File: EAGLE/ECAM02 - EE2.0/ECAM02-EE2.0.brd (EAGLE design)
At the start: 160 x 100 mm, 50 parts, among them J1 MODULAR TOOL, J2 SPI, J3 MOT, J4 FTDI, J5 S4B-PH-SM4, J6 S5B-PH-SM, J7 RINGLIGHT, Q2 16MHz, U1 SP3485, U2 ATMEGA238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

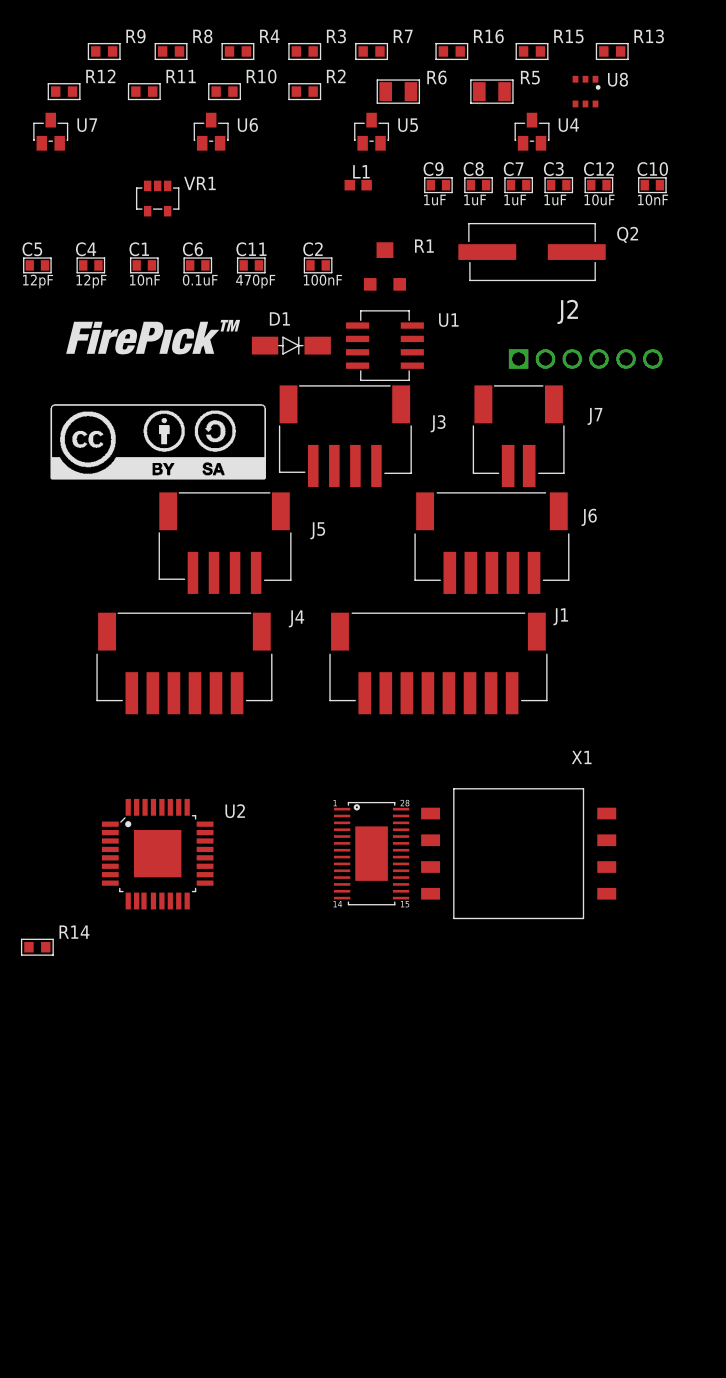
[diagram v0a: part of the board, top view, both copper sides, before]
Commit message: Finalized schematics (minus potential LDO regulator) for all boards. Layout partially done for EFD01
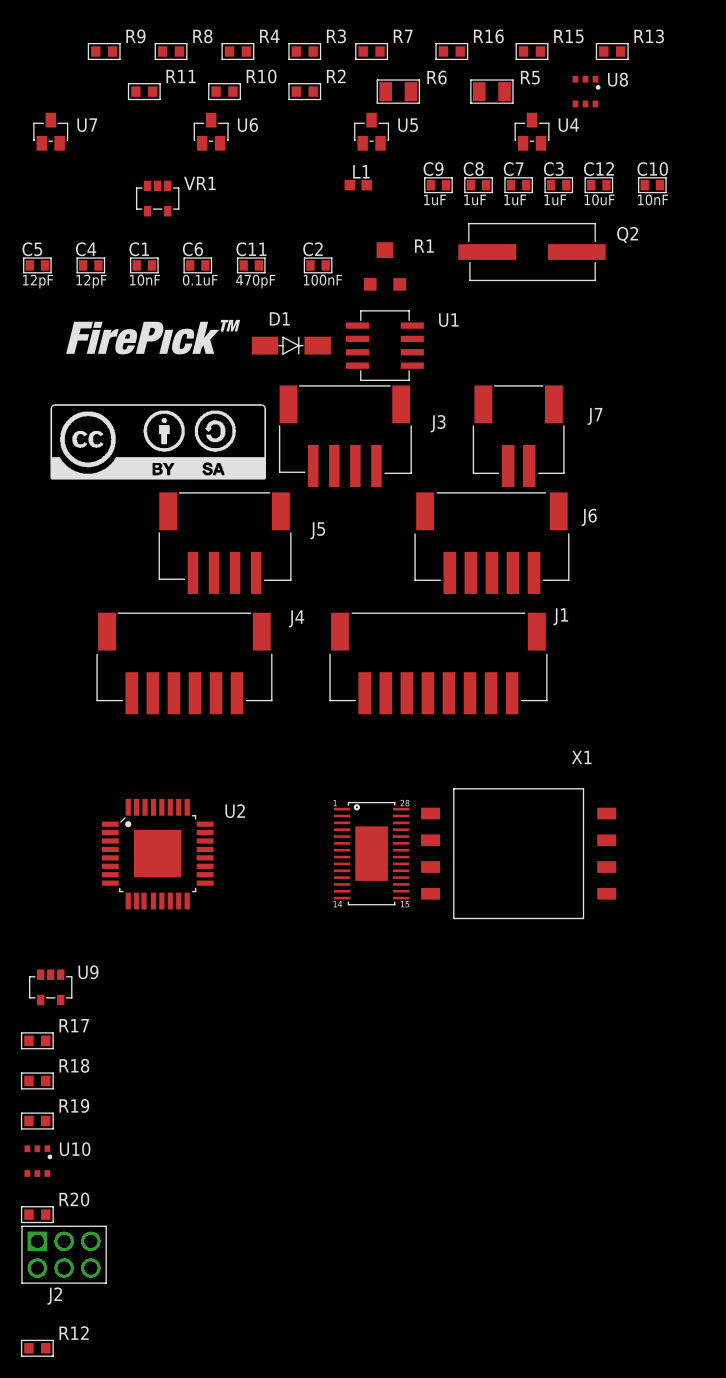
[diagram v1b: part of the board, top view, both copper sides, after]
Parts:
- removed R14: 10K, TinWhiskers:R0603
- added R17: 10R, TinWhiskers:R0603
- added R18, R20: 5K, TinWhiskers:R0603
- added R19: 90K, TinWhiskers:R0603
- added U10: MCP4725, TinWhiskers:SOT-23-6
- added U9: OR(74LVC), TinWhiskers:SOT-23-5
- J2: device TinWhiskers:CON-HDR-6POS-MALE -> TinWhiskers:CON-HDR-2X3P
- moved R12 119.4 mm to (-73.7, -40.6)
- moved J2 98.5 mm to (-71.1, -31.8)
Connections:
- removed net !ENBL: U2.9, U3.21
- removed net FB: J7.2, U8.3
- removed net SS: R14.2, U2.14
- new net !ENBL_AVR: U2.26, U9.2
- new net !ENBL_MOD: J1.2, U9.1
- new net A0: R19.1, U10.6
- new net N$10: R20.2, U10.1
- new net N$3: J7.2, R17.2, R18.2
- new net N$4: R18.1, R19.2, U8.3
- new net SCL: U10.5, U2.28
- new net SDA: U10.4, U2.27
- net !ENABLE: now also U3.21, U9.4; no longer J1.2
- net +3V3: now also U9.5
- net +5V: now also U10.3; no longer R14.1
- net CTRL: now also U2.11
- net DIR: now also U2.25
- net GATE1: now also U2.1; no longer U2.24
- net GATE2: now also U2.9; no longer U2.25
- net GATE3: now also U2.10; no longer U2.26
- net GATE4: now also U2.13; no longer U2.27
- net GND: now also R17.1, R20.1, U10.2, U9.3
- net STEP: now also U2.24; no longer U2.1

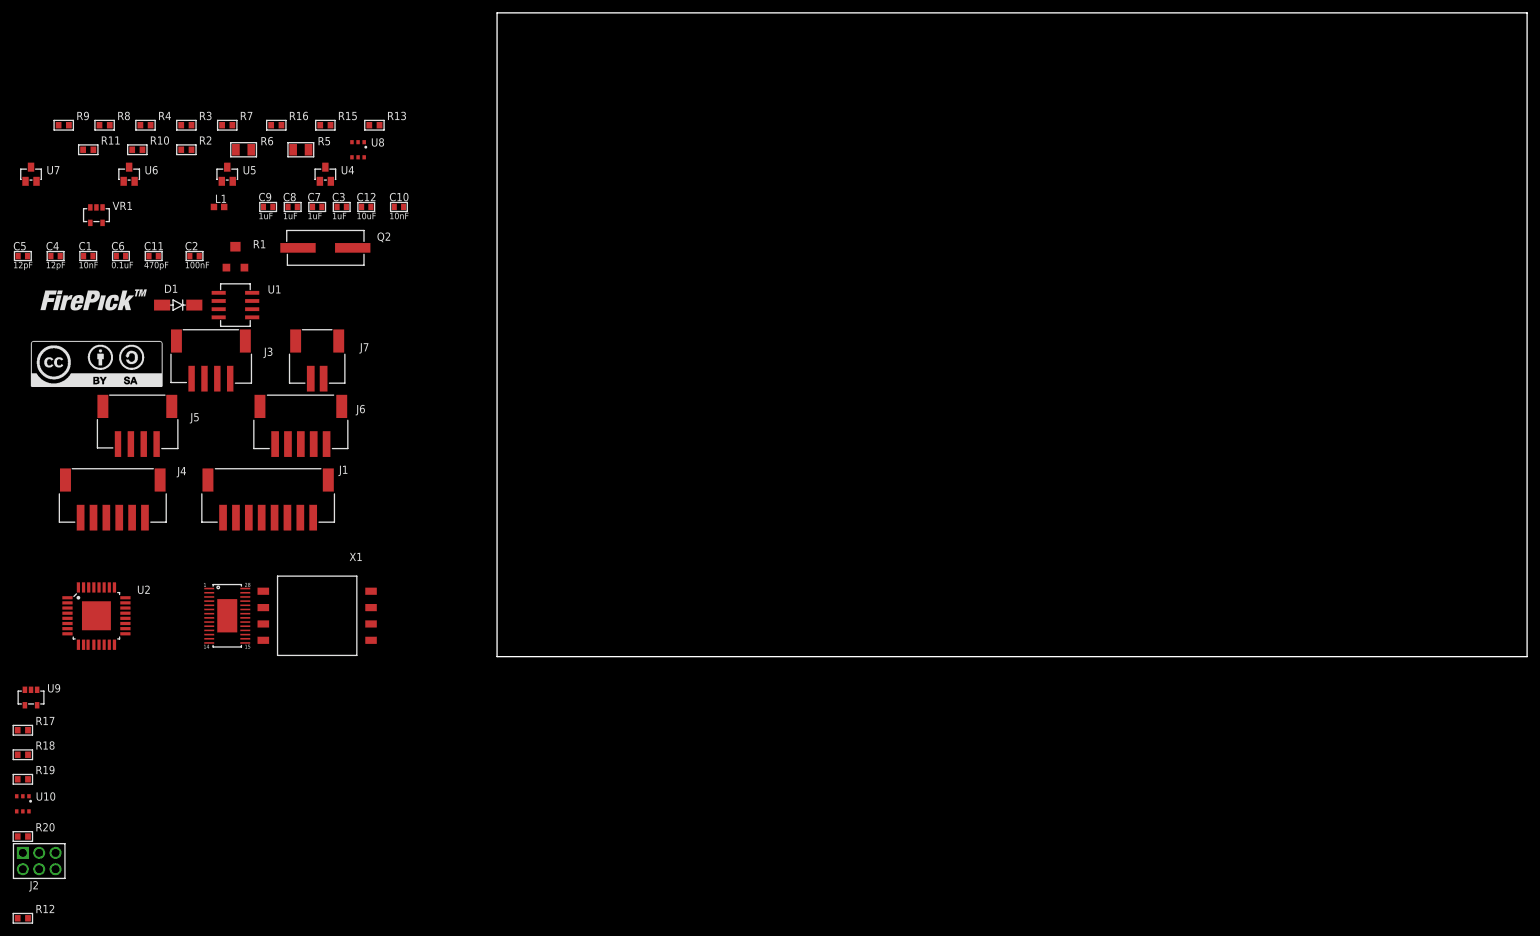
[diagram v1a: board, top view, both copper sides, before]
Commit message: Routed EFD01, ECAM03 boards. Modification needs to be made for hole/keepout in ECAM03. EMC03 X and Y sides routed. Will need to increase some trace widths.
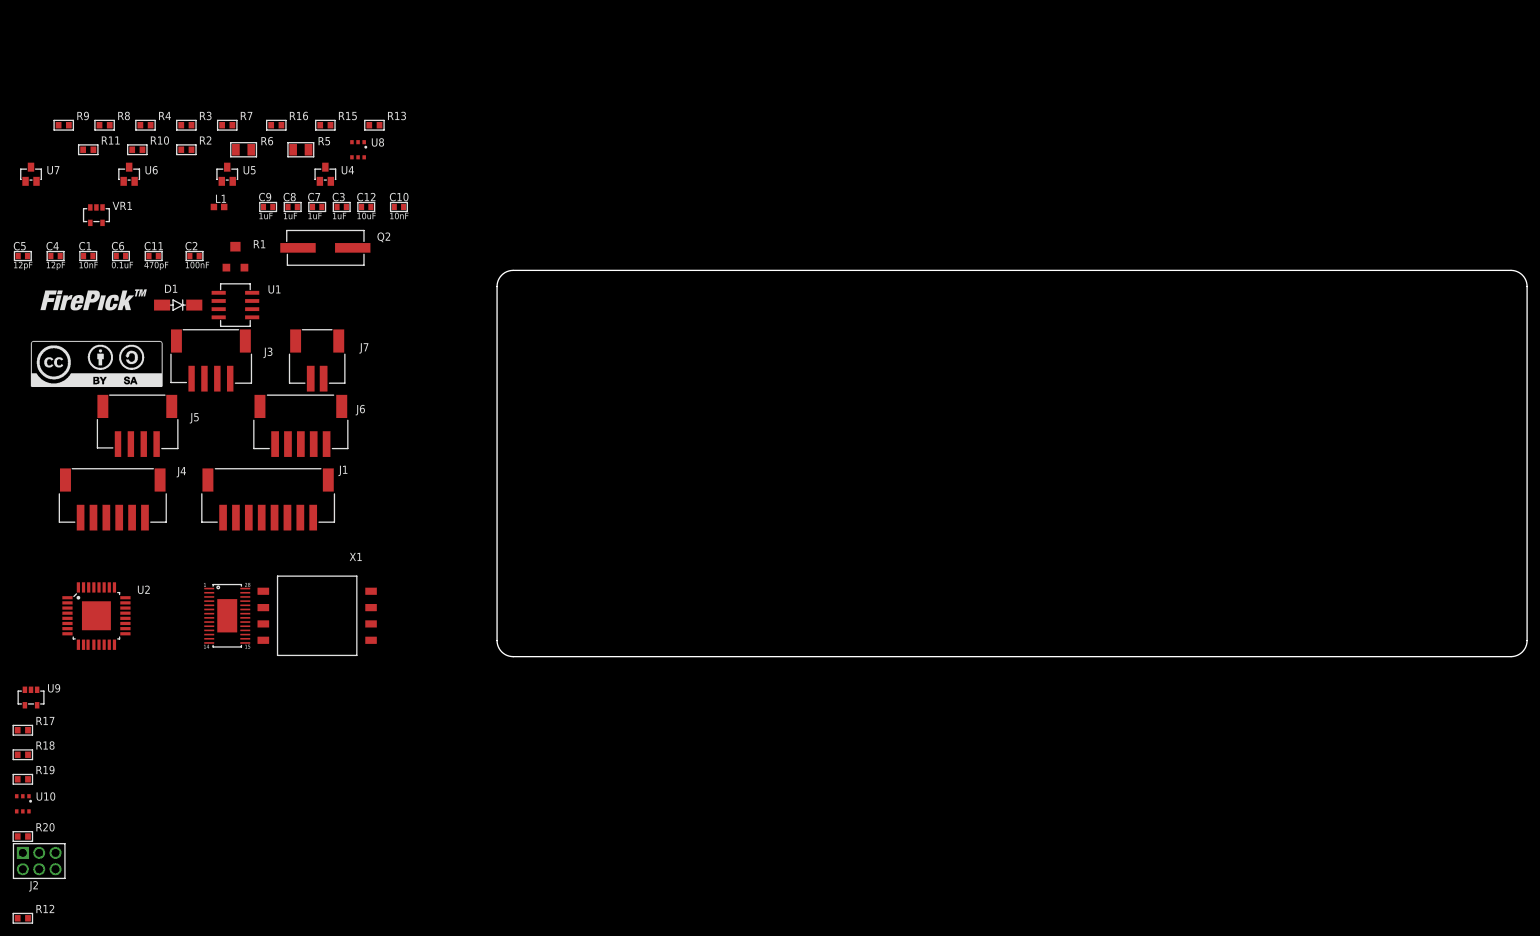
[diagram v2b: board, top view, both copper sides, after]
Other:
- board size 160 x 100 mm -> 160 x 60 mm
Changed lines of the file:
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@@
 <setting verticaltext="up"/>
 </settings>
-<grid distance="0.05" unitdist="inch" unit="inch" style="lines" multiple="1" display="no" altdistance="0.025" altunitdist="inch" altunit="inch"/>
+<grid distance="0.1" unitdist="mm" unit="mm" style="lines" multiple="1" display="no" altdistance="0.025" altunitdist="inch" altunit="mm"/>
 <layers>
 <layer number="1" name="Top" color="4" fill="1" visible="yes" active="yes"/>
@@
 <layer number="43" name="vRestrict" color="2" fill="10" visible="yes" active="yes"/>
 <layer number="44" name="Drills" color="7" fill="1" visible="no" active="yes"/>
-<layer number="45" name="Holes" color="7" fill="1" visible="no" active="yes"/>
+<layer number="45" name="Holes" color="7" fill="1" visible="yes" active="yes"/>
 <layer number="46" name="Milling" color="3" fill="1" visible="no" active="yes"/>
 <layer number="47" name="Measures" color="7" fill="1" visible="no" active="yes"/>
@@
 <board>
 <plain>
-<wire x1="0" y1="0" x2="160" y2="0" width="0" layer="20"/>
-<wire x1="160" y1="0" x2="160" y2="100" width="0" layer="20"/>
-<wire x1="160" y1="100" x2="0" y2="100" width="0" layer="20"/>
-<wire x1="0" y1="100" x2="0" y2="0" width="0" layer="20"/>
+<wire x1="0" y1="57.5" x2="0" y2="2.5" width="0.01" layer="20"/>
+<wire x1="0" y1="2.5" x2="2.5" y2="0" width="0.01" layer="20" curve="90"/>
+<wire x1="2.5" y1="0" x2="157.5" y2="0" width="0.01" layer="20"/>
+<wire x1="157.5" y1="0" x2="160" y2="2.5" width="0.01" layer="20" curve="90"/>
+<wire x1="160" y1="2.5" x2="160" y2="57.5" width="0.01" layer="20"/>
+<wire x1="160" y1="57.5" x2="157.5" y2="60" width="0.01" layer="20" curve="90"/>
+<wire x1="157.5" y1="60" x2="2.5" y2="60" width="0.01" layer="20"/>
+<wire x1="2.5" y1="60" x2="0" y2="57.5" width="0.01" layer="20" curve="90"/>
+<polygon width="0.01" layer="39">
+<vertex x="62.5" y="12.5"/>
+<vertex x="97.5" y="12.5"/>
+<vertex x="97.5" y="47.5"/>
+<vertex x="62.5" y="47.5"/>
+</polygon>
 </plain>
 <attributes>

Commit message: Routed all boards. EFP01 has a serious problem with spacing. Even on minimum allowable there are 300 DRC errors.
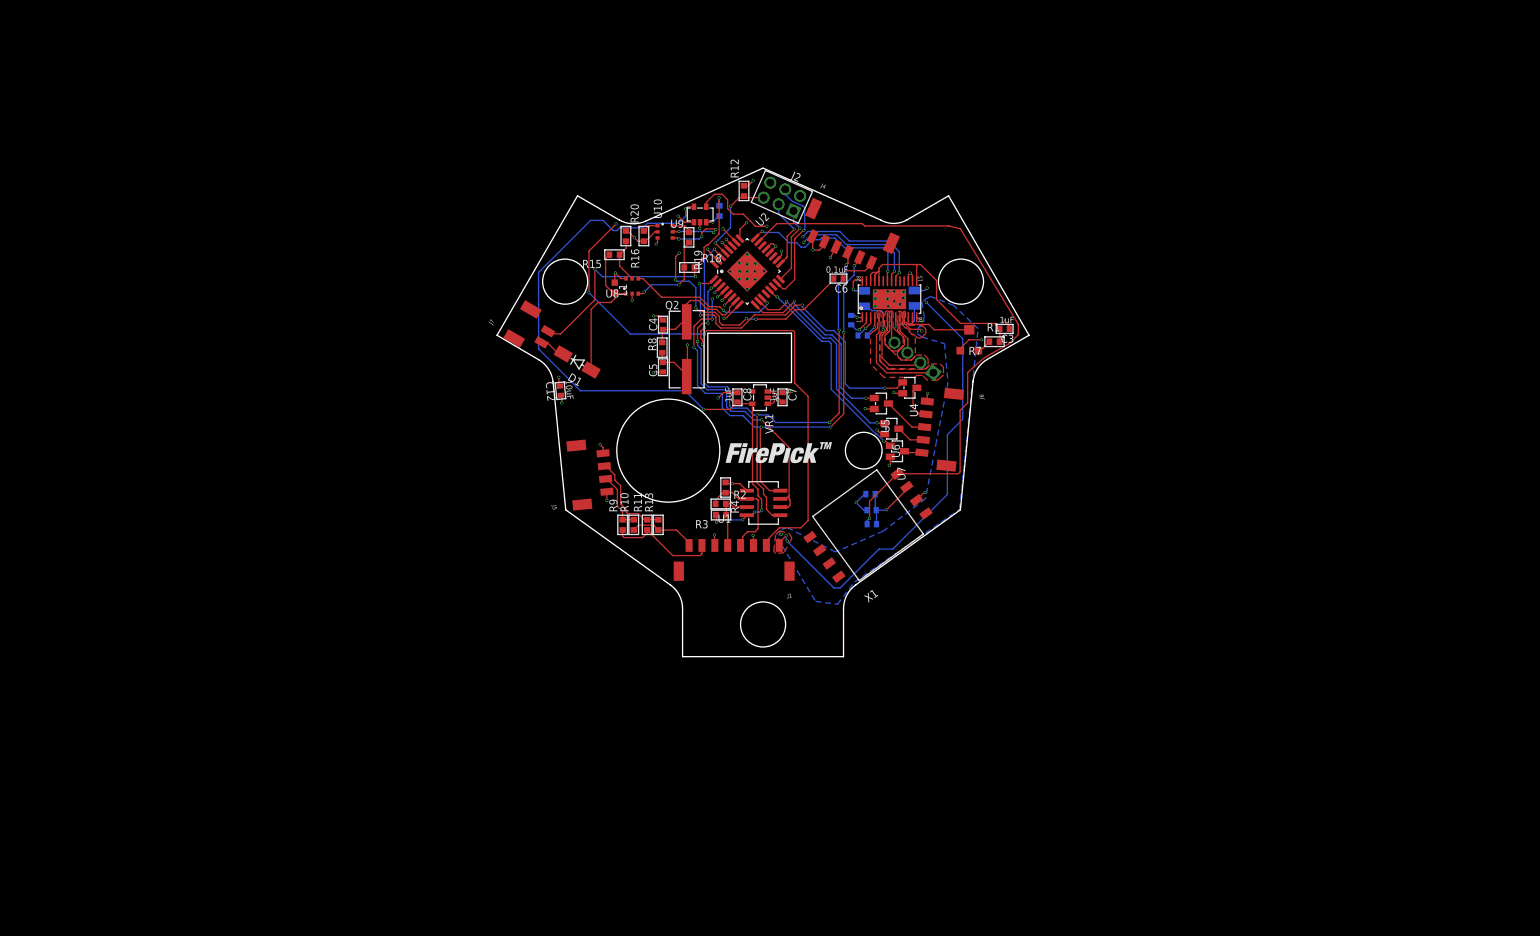
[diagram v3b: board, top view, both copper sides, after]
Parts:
- removed LOGO1: LOGO-CC-BY-SALARGE, FirePick:LOGO-CC-BY-SA
- J1: device TinWhiskers:CONN-JST-PH-2.0MM-8P-SMT-RA -> TinWhiskers:CON-JST-PH-2.0MM-8P-SMT-VRT
- J3: device TinWhiskers:CONN-JST-PH-2.0MM-4P-SMT-RA -> TinWhiskers:CON-HDR-4POS-MALE
- J4: device TinWhiskers:CONN-JST-PH-2.0MM-6P-SMT-RA -> TinWhiskers:CON-JST-PH-2.00MM-6P-SMT-VRT
- J5: device TinWhiskers:CONN-JST-PH-2.0MM-4P-SMT-RA -> TinWhiskers:CON-JST-PH-2.0MM-4P-SMT-VRT
- J6: device TinWhiskers:CONN-JST-PH-2.0MM-5P-SMT-RA -> TinWhiskers:CON-JST-PH-2.0MM-5P-SMT-VRT
- J7: device TinWhiskers:CONN-JST-PH-2.0MM-2P-SMT-RA -> TinWhiskers:CON-JST-PH-2.0MM-2P-SMT-VRT
- moved R12 159.1 mm to (38.4, 72.3), turned to 90 degrees
- moved J2 154.8 mm to (44.2, 71.4), turned to 156 degrees
- moved U7 141.3 mm to (62.2, 31.9), turned to 270 degrees
- moved R17 135.0 mm to (34.5, 69.2), flipped to the bottom, turned to 90 degrees
- moved R20 134.2 mm to (22.8, 65.3), turned to 90 degrees
- moved U10 133.6 mm to (26.1, 66.0), turned to 90 degrees
- moved R19 133.4 mm to (29.8, 65.1), turned to 270 degrees
- moved R18 128.2 mm to (29.9, 60.5)
- moved U9 128.2 mm to (31.5, 68.7), turned to 180 degrees
- moved U6 124.9 mm to (61.3, 35.4), turned to 270 degrees
- moved R7 123.8 mm to (77.3, 48.9), turned to 180 degrees
- moved J4 120.7 mm to (53.6, 63.2), turned to 336 degrees
- moved C11 119.1 mm to (58.2, 20.6), flipped to the bottom
- moved C1 118.9 mm to (55.0, 52.3), flipped to the bottom, turned to 90 degrees
- moved R1 114.7 mm to (73.4, 49.3)
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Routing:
- net +3V3: track 0.00 -> 106.0 mm, vias 0 -> 6
- net !ENBL_MOD: track 0.00 -> 99.8 mm, vias 0 -> 4
- net VOUT: track 0.00 -> 97.1 mm, vias 0 -> 1
- net RO: track 0.00 -> 92.6 mm, vias 0 -> 7
- net DI: track 0.00 -> 91.5 mm, vias 0 -> 8
- net +24V: track 0.00 -> 87.1 mm, vias 0 -> 6
- net GND: track 0.00 -> 67.5 mm, vias 0 -> 49
- net RESET: track 0.00 -> 60.3 mm, vias 0 -> 7
- net GATE1: track 0.00 -> 51.5 mm, vias 0 -> 4
- net DTR1: track 0.00 -> 49.2 mm, vias 0 -> 4
- net N$3: track 0.00 -> 45.8 mm, vias 0 -> 3
- net !ENABLE: track 0.00 -> 40.5 mm, vias 0 -> 3
- net N$13: track 0.00 -> 35.6 mm
- net DIR: track 0.00 -> 34.0 mm, vias 0 -> 3
- net +5V: track 0.00 -> 33.1 mm, vias 0 -> 15
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- added copper zone on layer 1, net +24V
- added copper zone on layer 15, net +24V
- added copper zone on layer 16, net +24V
- added copper zone on layer 15, net +5V
- added copper zone on layer 1, net AOUT1
- added copper zone on layer 1, net AOUT2
- added copper zone on layer 1, net BOUT1
- added copper zone on layer 1, net BOUT2
- added copper zone on layer 2, net GND
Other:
- board size 160 x 60 mm -> 82.6 x 75.9 mm
